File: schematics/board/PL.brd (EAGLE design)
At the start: 82 x 92 mm, 118 parts, among them U1 STM32F405RGT6, U2 LMC555CMX/NOPB

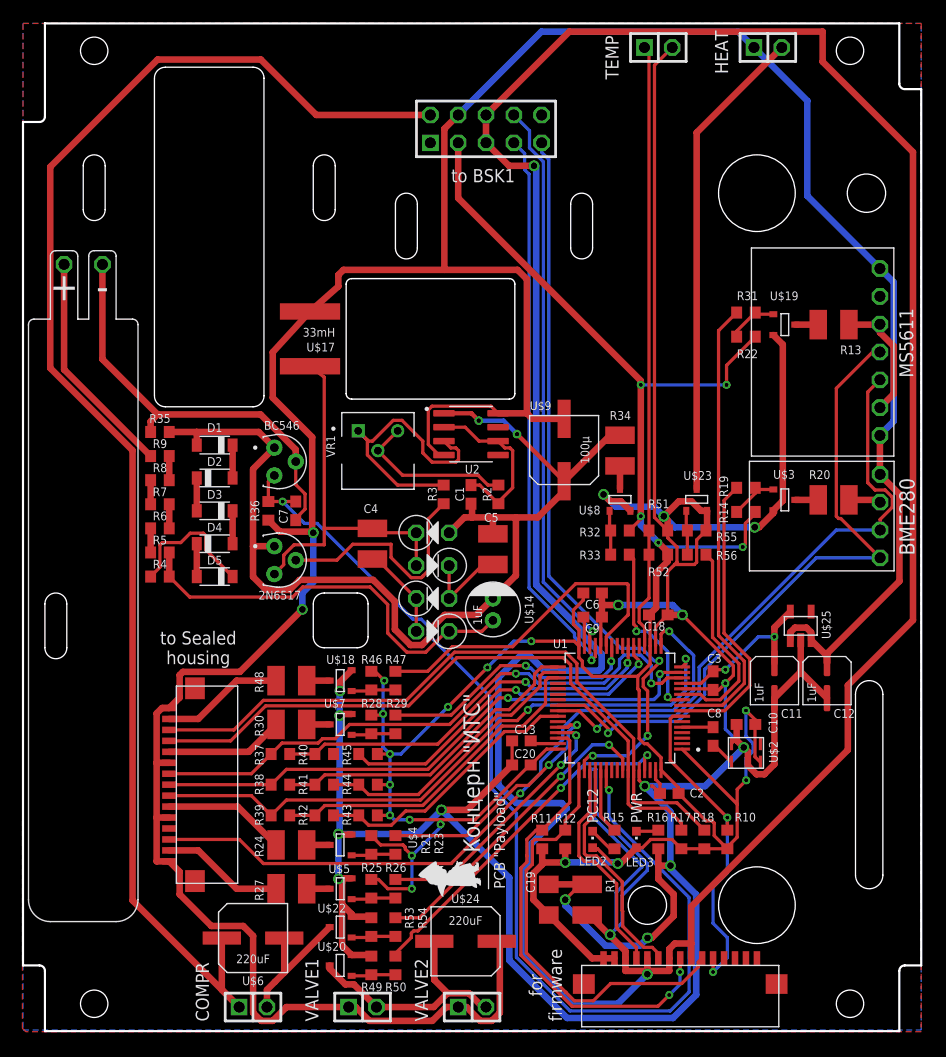
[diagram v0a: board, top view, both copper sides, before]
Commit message: Замечания по плате ПН устранены
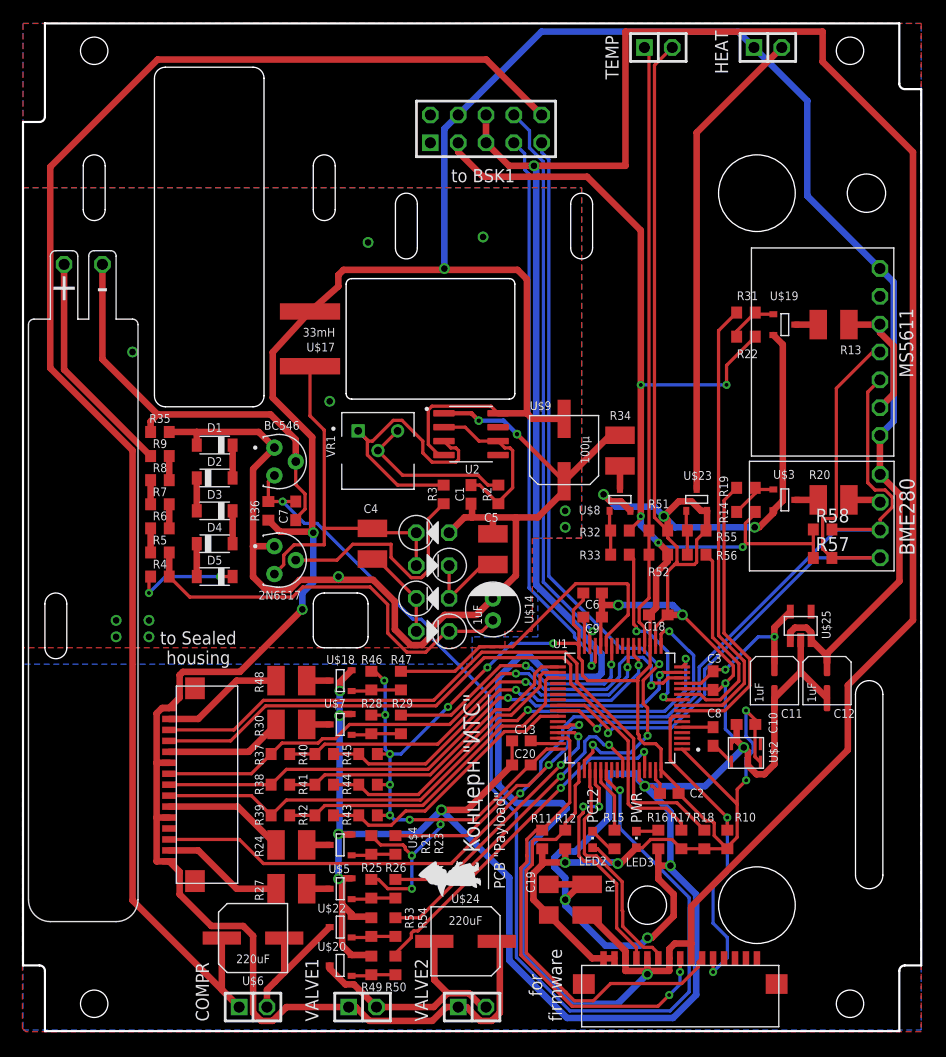
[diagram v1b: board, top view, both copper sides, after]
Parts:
- added R57, R58: 5k1, resistor:R0603
- moved R29 0.50 mm to (34.5, 28.0)
- moved R47 0.50 mm to (34.5, 32.0)
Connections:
- net 3V3: now also R57.1, R58.1
- net BUS+: now also BSK1.10; no longer BSK1.2
- net RX-S: now also U1.52; no longer U1.51
- net SENS-EXT-SCL: now also R58.2
- net SENS-EXT-SDA: now also R57.2
- net TX-S: now also U1.51; no longer U1.52
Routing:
- net GND-OUT: track 296.6 -> 265.5 mm, vias 3 -> 2
- net GND: track 321.9 -> 340.6 mm
- net 3V3: track 255.0 -> 270.7 mm
- net BUS+: track 131.7 -> 141.8 mm
- net SENS-EXT-SCL: track 55.1 -> 59.5 mm
- net SENS-EXT-SDA: track 61.3 -> 65.5 mm
- net CTRL-NO2-2: track 31.9 -> 35.1 mm
- net N$27: track 12.7 -> 9.82 mm, vias 0 -> 2
- net RX-S: track 20.3 -> 21.6 mm, vias 0 -> 2
- net COMPR: track 28.9 -> 30.1 mm
- net CTRL-NO2-1: track 36.6 -> 37.7 mm
- net SCL-TM: track 51.6 -> 52.6 mm
- net TIME: track 68.3 -> 69.1 mm
- net NO2: track 54.7 -> 55.5 mm
- net DOSIM: track 16.5 -> 17.0 mm
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- added copper zone on layer 1, net DOS-G
- added copper zone on layer 16, net DOS-G

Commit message: Добавлены герберы плат BSK1-4, PL, SP и SPIDER
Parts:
- U2: value LMC555CMX/NOPB -> LMC555
- moved U$6 0.50 mm to (21.0, 8.00)
- renumbered LED2 to LED-B, LED3 to LED-G, U$18 to SI2302-5, U$19 to SI2302-1, U$2 to Q24, U$20 to SI2302-0, U$22 to SI2302-9, U$23 to SI2302-3, U$25 to STAB, U$3 to SI2302-2, U$4 to SI2302-7, U$5 to SI2302-8, U$7 to SI2302-6, U$8 to SI2302-4
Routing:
- net GND-COMPR: track 12.8 -> 12.3 mm
- net BUS+: track 141.8 -> 141.3 mm
